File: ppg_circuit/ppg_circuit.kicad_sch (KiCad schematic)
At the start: 25 parts, among them U1 ${SIM.PARAMS}, U2 ${SIM.PARAMS}

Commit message: added footprints to circuit and finalized it
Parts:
- removed C2: 10u, symbol Device:C
- removed C4: 100u, symbol Device:C
- removed U1, U2: ${SIM.PARAMS}, symbol Simulation_SPICE:OPAMP
- removed V2, V3, V4, V5: 1.65, symbol Simulation_SPICE:VDC
- added C1: 10u, Capacitor_THT:CP_Radial_D5.0mm_P2.00mm, symbol Device:C_Polarized
- added C2: 100u, Capacitor_THT:CP_Radial_D6.3mm_P2.50mm, symbol Device:C_Polarized
- added U1: Opamp_Dual, Package_DIP:DIP-8_W7.62mm_Socket, symbol Amplifier_Operational:Opamp_Dual
- added U2: MCP6001x-LT, Package_DIP:DIP-8_W7.62mm_Socket, symbol Amplifier_Operational:MCP6001x-LT
- C3: footprint (none) -> Capacitor_THT:C_Disc_D3.0mm_W1.6mm_P2.50mm
- C4: renamed from C1; footprint (none) -> Capacitor_THT:C_Disc_D3.0mm_W1.6mm_P2.50mm
- R1: renamed from R2; value 0 -> 10k; footprint (none) -> Resistor_THT:R_Axial_DIN0207_L6.3mm_D2.5mm_P10.16mm_Horizontal
- R2: renamed from R3; footprint (none) -> Resistor_THT:R_Axial_DIN0207_L6.3mm_D2.5mm_P10.16mm_Horizontal
- R3: renamed from R5; footprint (none) -> Resistor_THT:R_Axial_DIN0207_L6.3mm_D2.5mm_P10.16mm_Horizontal
- R4: footprint (none) -> Resistor_THT:R_Axial_DIN0207_L6.3mm_D2.5mm_P10.16mm_Horizontal
- R5: renamed from R6; footprint (none) -> Resistor_THT:R_Axial_DIN0207_L6.3mm_D2.5mm_P10.16mm_Horizontal
- R6: renamed from R7; footprint (none) -> Resistor_THT:R_Axial_DIN0207_L6.3mm_D2.5mm_P10.16mm_Horizontal
- R7: renamed from R8; footprint (none) -> Resistor_THT:R_Axial_DIN0207_L6.3mm_D2.5mm_P10.16mm_Horizontal
- renumbered D2 to D1, D1 to D2, R1 to R_L1
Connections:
- net GND: now also C1.2, U1.3 (+), U1.5 (+), U2.3 (+)
- net high: now also R7.2, U1.8 (V+), U2.5 (V+); no longer R6.1
- net in: now also C3.2, U1.2 (-); no longer C3.1
- net low: now also R6.1, U1.4 (V-), U2.2 (V-); no longer R7.2
- net out1: now also C3.1, U1.1; no longer C3.2
- net out2: now also C1.1, C2.1
- net out3: now also C2.2
- net outf: now also U1.7
- net at C4.2, R4.2, R5.2: now also U1.6 (-)
- new net ground: U2.1, U2.4 (-)
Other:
- note added: "voltage divider"
- moved on the sheet: C4, R1, R5, R6, R7, V6

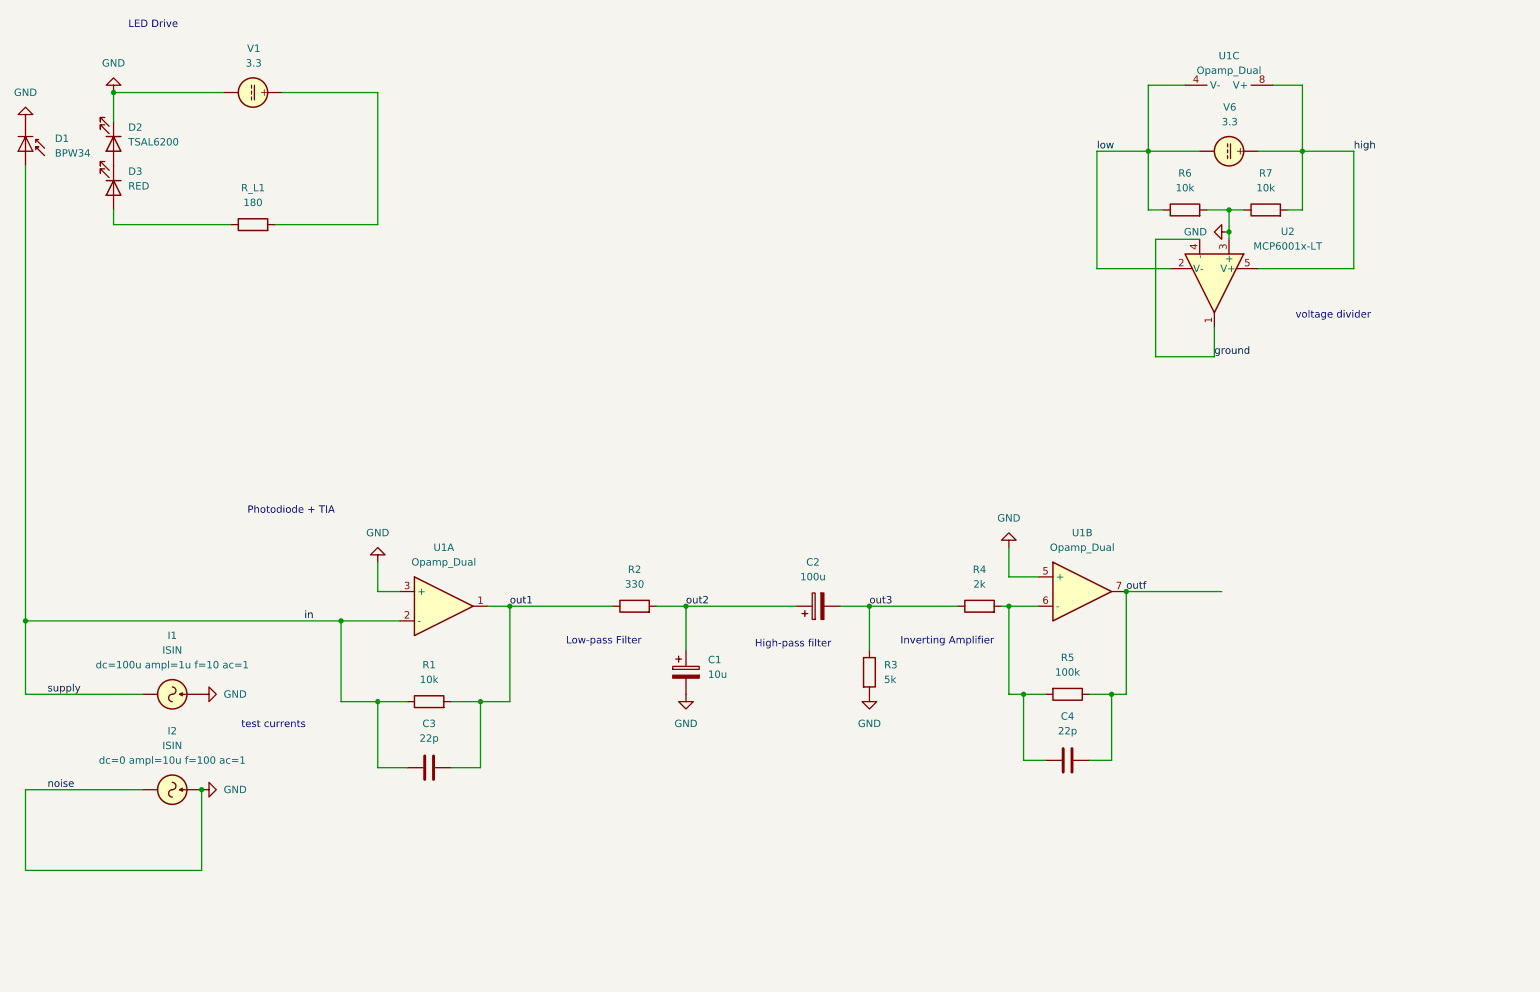
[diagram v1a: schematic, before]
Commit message: designed pcb, added teensy to the design
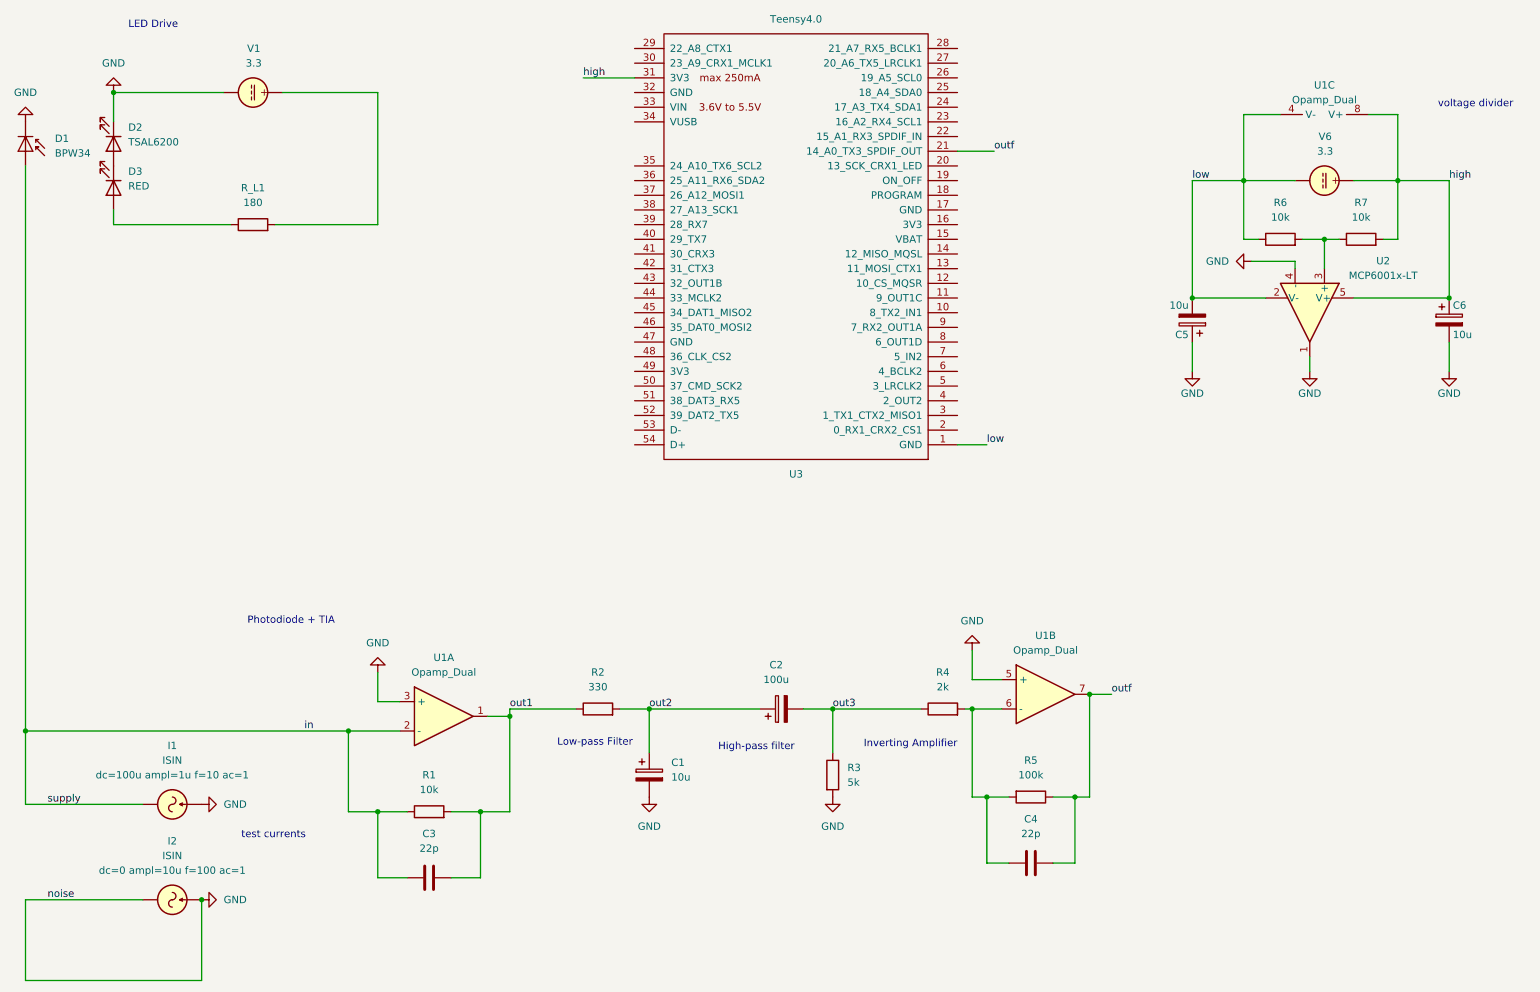
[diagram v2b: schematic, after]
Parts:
- added C5, C6: 10u, Capacitor_THT:CP_Radial_D5.0mm_P2.00mm, symbol Device:C_Polarized
- added U3: Teensy4.0, teensy:Teensy40, symbol teensy:Teensy4.0
- U1: private KLC_S6.2 -> KLC_S3.1; private_1 (none) -> KLC_S4.1; private_2 (none) -> KLC_S6.2
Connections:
- net ground is gone; now on net GND: U2.1, U2.4 (-)
- net GND: now also C5.1, C6.2; no longer R6.2, R7.1, U2.3 (+)
- net high: now also C6.1, U3.31 (3V3)
- net low: now also C5.2, U3.1 (GND)
- net outf: now also U3.21 (14_A0_TX3_SPDIF_OUT)
- new net: R6.2, R7.1, U2.3 (+)
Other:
- moved on the sheet: C1, C2, C3, C4, I1, I2, R1, R2, R3, R4, R5, R6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

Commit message: fixed errors in pcb and moved the photodiode so it is more accessable on the pcb
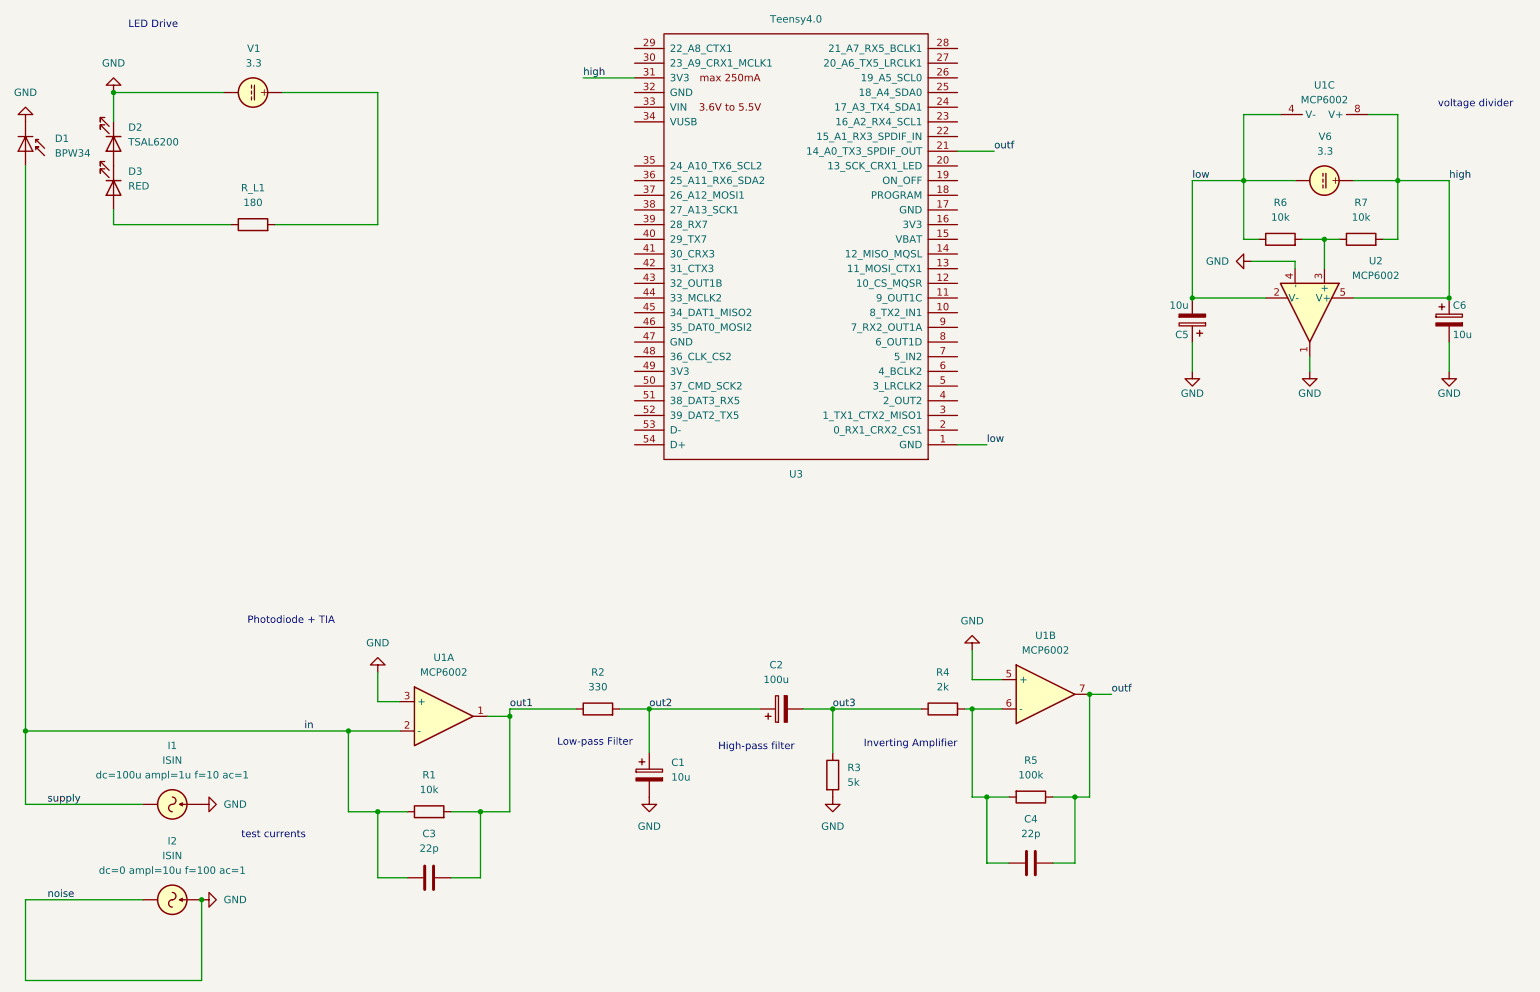
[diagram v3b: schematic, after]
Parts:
- U1: value Opamp_Dual -> MCP6002
- U2: value MCP6001x-LT -> MCP6002
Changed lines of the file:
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@@
 			)
 		)
-		(property "Value" "Opamp_Dual"
+		(property "Value" "MCP6002"
 			(at 90.17 128.27 0)
 			(show_name no)
@@
 		(fields_autoplaced yes)
 		(property "Reference" "U2"
-			(at 252.73 57.0798 90)
-			(show_name no)
-			(do_not_autoplace no)
-			(effects
-				(font
-					(size 1.27 1.27)
-				)
-			)
-		)
-		(property "Value" "MCP6001x-LT"
-			(at 252.73 59.6198 90)
+			(at 251.46 57.0798 90)
+			(show_name no)
+			(do_not_autoplace no)
+			(effects
+				(font
+					(size 1.27 1.27)
+				)
+			)
+		)
+		(property "Value" "MCP6002"
+			(at 251.46 59.6198 90)
 			(show_name no)
 			(do_not_autoplace no)
@@
 			)
 		)
-		(property "Value" "Opamp_Dual"
+		(property "Value" "MCP6002"
 			(at 242.57 29.21 90)
 			(show_name no)
@@
 			)
 		)
-		(property "Value" "Opamp_Dual"
+		(property "Value" "MCP6002"
 			(at 194.31 124.46 0)
 			(show_name no)
